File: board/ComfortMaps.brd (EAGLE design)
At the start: 96.8 x 49.3 mm, 48 parts, among them J1 PROG_HDR, J5 0545482271, J6 0545482271, U1 ADXL362, U3 ADP160-3.3, U4 MCP73833, X1 RASPI_GPIO_B+#_PIN

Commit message: Latest, before upwork.
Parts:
- removed JP1: FTDI_DEVICE, SparkFun-Connectors:FTDI_DEVICE_SIDE
- moved X1 8.89 mm to (39.8, 7.24)
- moved D5 7.91 mm to (72.9, 27.2)
- moved D3 7.88 mm to (72.9, 30.7)
- moved D4 7.88 mm to (72.9, 29.0)
- moved J1 6.37 mm to (19.8, 32.8)
- moved C5 3.78 mm to (65.0, 30.5)
- moved C3 3.45 mm to (23.5, 1.78)
- moved R5 3.07 mm to (77.0, 27.2)
- moved R6 3.07 mm to (77.0, 29.0)
- moved R7 3.07 mm to (77.0, 30.6)
- moved J4 1.78 mm to (9.65, 5.08)
- moved J2 0.15 mm to (10.9, -2.13)
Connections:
- new net TX0: X1.10
- net GND: no longer JP1.P$6
- net RXI: now also X1.8; no longer JP1.P$3
- net TXO: no longer JP1.P$2
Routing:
- net TXO: track 41.1 -> 5.68 mm
- net GPIO18: track 67.9 -> 102.7 mm
- net GND: track 375.8 -> 350.0 mm
- net VOUT: track 32.6 -> 51.3 mm
- net GPIO23: track 44.8 -> 59.2 mm, vias 2 -> 3
- net OVERRIDE: track 58.0 -> 48.8 mm
- net RESET: track 33.4 -> 26.8 mm
- net SCK: track 44.2 -> 37.6 mm
- net MOSI: track 43.5 -> 36.9 mm
- net MISO: track 39.4 -> 32.9 mm
- net V_USB: track 67.1 -> 73.6 mm
- net RXI: track 56.2 -> 62.2 mm
- net N$11: track 8.26 -> 2.34 mm, vias 2 -> 0
- net N$10: track 8.05 -> 2.34 mm, vias 2 -> 0
- net GPIO27: track 51.5 -> 57.0 mm
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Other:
- board text added: "Comfort Maps Samuel Clay V2 2019-12-26"
- board text removed: "Comfort Maps Samuel Clay V1 2019-11-22"

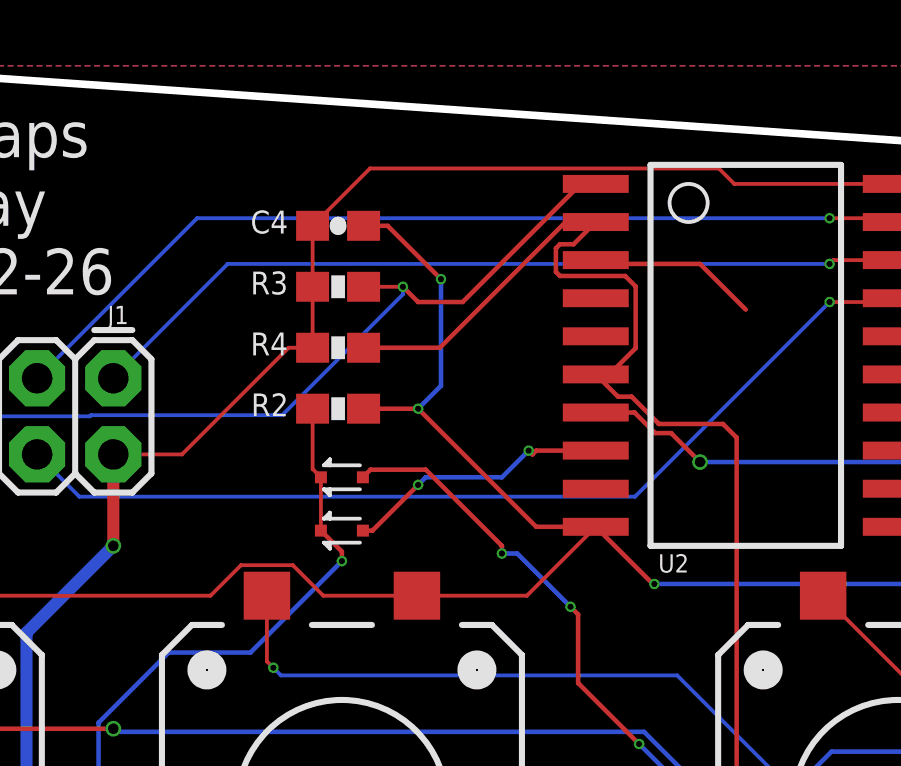
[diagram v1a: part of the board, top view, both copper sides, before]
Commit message: Switching to larger schottke diode.
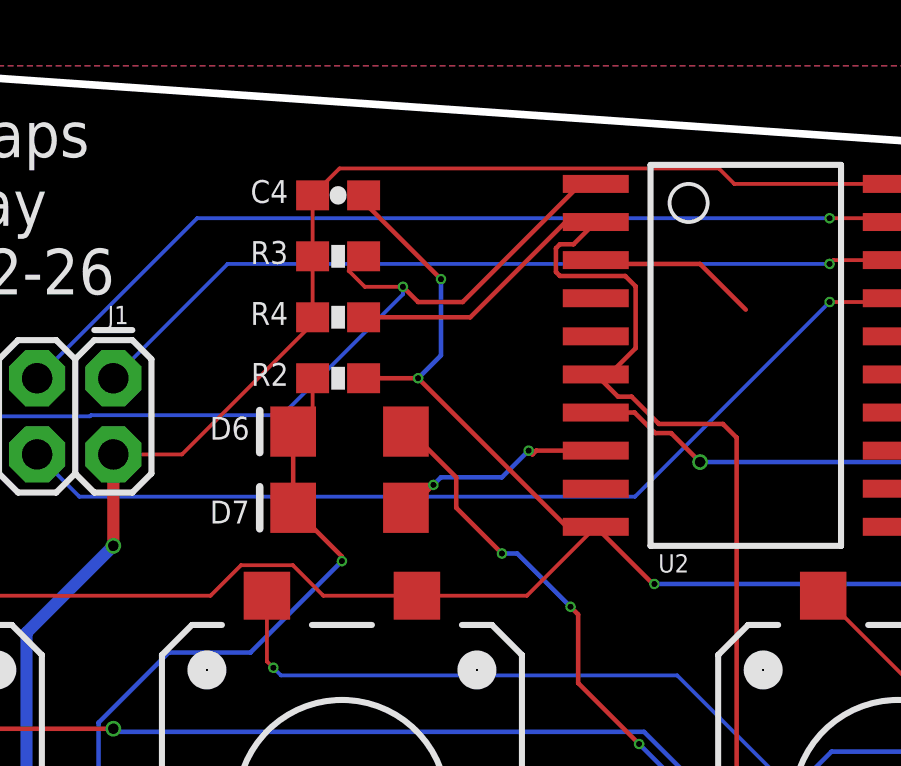
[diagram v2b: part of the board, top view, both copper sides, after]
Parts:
- removed D1, D2: RB751, SparkFun-DiscreteSemi:SOD-523
- added D6, D7: SS14-LTP_SCHOTTKY_DIODE_SMT_DO-214AC, DIODE SCHOTTKY 1A 40V SMA:DO-214AC
- moved C4 1.02 mm to (27.3, 38.9)
- moved R4 1.02 mm to (27.3, 34.8)
- moved R2 1.02 mm to (27.3, 32.8)
- moved R3 1.02 mm to (27.3, 36.8)
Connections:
- net ACTIVE: now also D7.A; no longer D2.A
- net N$2: now also D6.C, D7.C; no longer D1.C, D2.C
- net OVERRIDE: now also D6.A; no longer D1.A
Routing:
- net N$2: track 75.5 -> 77.6 mm
- net ACTIVE: track 8.97 -> 7.22 mm
- net RESET: track 26.8 -> 28.2 mm
- net OVERRIDE: track 48.8 -> 48.3 mm

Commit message: v3 of the board, with new mounting holes and an added LED for V_out.
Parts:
- removed J5, J6: 0545482271, 0545482271:0545482271
- added D1: RED, SparkFun-LED:LED-0603
- added R17: 1.5k, SparkFun-Resistors:0603
- moved U$3 9.14 mm to (6.27, 0.28)
- moved C4 2.74 mm to (29.8, 39.9)
- moved R2 2.74 mm to (29.8, 33.8)
- moved R3 2.74 mm to (29.8, 37.8)
- moved R4 2.74 mm to (29.8, 35.8)
- moved C2 2.55 mm to (26.3, -2.03)
- moved C3 2.55 mm to (26.0, 2.03)
- moved J2 2.55 mm to (13.5, -1.88)
- moved U3 2.55 mm to (21.1, 0.38)
- moved J4 1.37 mm to (9.14, 6.35)
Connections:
- removed net CSI1: J5.1, J6.1
- removed net CSI10: J5.10, J6.10
- removed net CSI11: J5.11, J6.11
- removed net CSI12: J5.12, J6.12
- removed net CSI13: J5.13, J6.13
- removed net CSI14: J5.14, J6.14
- removed net CSI15: J5.15, J6.15
- removed net CSI16: J5.16, J6.16
- removed net CSI17: J5.17, J6.17
- removed net CSI18: J5.18, J6.18
- removed net CSI19: J5.19, J6.19
- removed net CSI2: J5.2, J6.2
- removed net CSI20: J5.20, J6.20
- removed net CSI21: J5.21, J6.21
- removed net CSI22: J5.22, J6.22
- removed net CSI23: J5.23, J6.23
- removed net CSI24: J5.24, J6.24
- removed net CSI3: J5.3, J6.3
- removed net CSI4: J5.4, J6.4
- removed net CSI5: J5.5, J6.5
- removed net CSI6: J5.6, J6.6
- removed net CSI7: J5.7, J6.7
- removed net CSI8: J5.8, J6.8
- removed net CSI9: J5.9, J6.9
- new net N$14: D1.C, R17.1
- net GND: now also R17.2
- net VOUT: now also D1.A
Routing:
- net VOUT: track 51.3 -> 66.2 mm
- net N$14: track 0.00 -> 7.64 mm
- net CSI24: track 7.62 -> 0.00 mm
- net CSI23: track 7.62 -> 0.00 mm
- net CSI9: track 7.62 -> 0.00 mm
- net CSI8: track 7.62 -> 0.00 mm
- net CSI7: track 7.62 -> 0.00 mm
- net CSI6: track 7.62 -> 0.00 mm
- net CSI5: track 7.62 -> 0.00 mm
- net CSI4: track 7.62 -> 0.00 mm
- net CSI3: track 7.62 -> 0.00 mm
- net CSI22: track 7.62 -> 0.00 mm
- net CSI21: track 7.62 -> 0.00 mm
- net CSI20: track 7.62 -> 0.00 mm
- net CSI2: track 7.62 -> 0.00 mm
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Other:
- board text added: "Comfort Maps Samuel Clay V3 2020-01-27"
- board text removed: "Comfort Maps Samuel Clay V2 2019-12-26"
